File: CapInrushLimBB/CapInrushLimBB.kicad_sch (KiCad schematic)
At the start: 35 parts, among them J1 Screw_Terminal_01x02, J2 Screw_Terminal_01x02, J3 Screw_Terminal_01x02, K1 G5LE-1, Q1 IRF9540N, Q2 Q_PMOS_GDSD, Q3 MPSA42, Q4 MPSA42

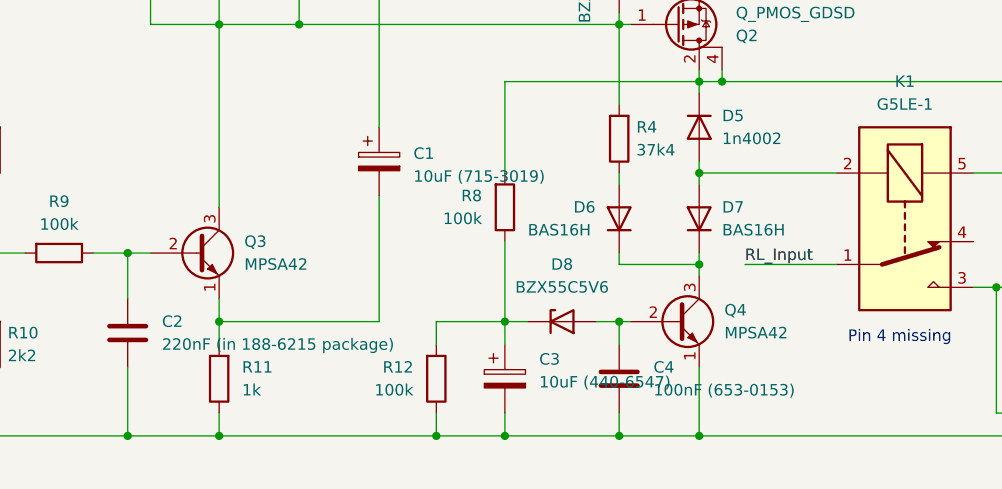
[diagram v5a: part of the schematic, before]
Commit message: Tweaked component values (names) and checked footprints.
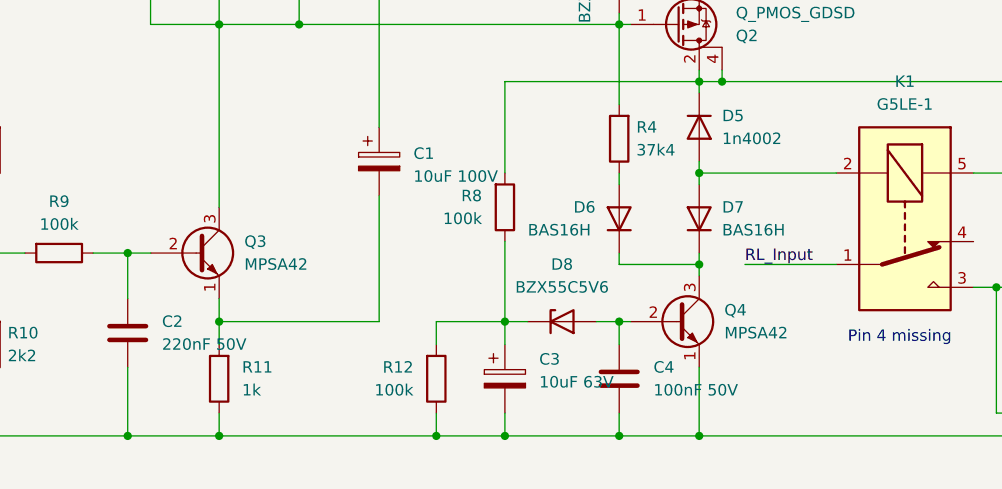
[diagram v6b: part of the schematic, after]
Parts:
- C1: value 10uF (715-3019) -> 10uF 100V
- C2: value 220nF (in 188-6215 package) -> 220nF 50V
- C3: value 10uF (440-6547) -> 10uF 63V
- C4: value 100nF (653-0153) -> 100nF 50V
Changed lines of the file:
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@@
       (effects (font (size 1.27 1.27)) (justify left))
     )
-    (property "Value" "10uF (715-3019)" (id 1) (at 115.57 110.8709 0)
+    (property "Value" "10uF 100V" (id 1) (at 115.57 110.8709 0)
       (effects (font (size 1.27 1.27)) (justify left))
     )
@@
       (effects (font (size 1.27 1.27)) (justify left))
     )
-    (property "Value" "220nF (in 188-6215 package)" (id 1) (at 87.63 129.5399 0)
+    (property "Value" "220nF 50V" (id 1) (at 87.63 129.5399 0)
       (effects (font (size 1.27 1.27)) (justify left))
     )
@@
       (effects (font (size 1.27 1.27)) (justify left))
     )
-    (property "Value" "100nF (653-0153)" (id 1) (at 142.24 134.6199 0)
+    (property "Value" "100nF 50V" (id 1) (at 142.24 134.6199 0)
       (effects (font (size 1.27 1.27)) (justify left))
     )
@@
       (effects (font (size 1.27 1.27)) (justify left))
     )
-    (property "Value" "10uF (440-6547)" (id 1) (at 129.54 133.7309 0)
+    (property "Value" "10uF 63V" (id 1) (at 129.54 133.7309 0)
       (effects (font (size 1.27 1.27)) (justify left))
     )
@@
   (symbol_instances
     (path "/4700c50c-9860-4532-a2c7-53fd9c745d97"
-      (reference "C1") (unit 1) (value "10uF (715-3019)") (footprint "Capacitor_THT:CP_Radial_D6.3mm_P2.50mm")
+      (reference "C1") (unit 1) (value "10uF 100V") (footprint "Capacitor_THT:CP_Radial_D6.3mm_P2.50mm")
     )
     (path "/aa3000e9-ae89-4921-813a-5088ef73c282"
-      (reference "C2") (unit 1) (value "220nF (in 188-6215 package)") (footprint "Capacitor_THT:C_Disc_D5.1mm_W3.2mm_P5.00mm")
+      (reference "C2") (unit 1) (value "220nF 50V") (footprint "Capacitor_THT:C_Disc_D5.1mm_W3.2mm_P5.00mm")
     )
     (path "/d60a5db2-8cd8-4af1-8cbf-01714930ea15"
-      (reference "C3") (unit 1) (value "10uF (440-6547)") (footprint "Capacitor_THT:CP_Radial_D5.0mm_P2.00mm")
+      (reference "C3") (unit 1) (value "10uF 63V") (footprint "Capacitor_THT:CP_Radial_D5.0mm_P2.00mm")
     )
     (path "/c42c87d9-6630-4bdd-b504-0fc4fcaddf1b"
-      (reference "C4") (unit 1) (value "100nF (653-0153)") (footprint "Capacitor_THT:C_Disc_D5.1mm_W3.2mm_P5.00mm")
+      (reference "C4") (unit 1) (value "100nF 50V") (footprint "Capacitor_THT:C_Disc_D5.1mm_W3.2mm_P5.00mm")
     )
     (path "/3d73d65c-87b2-4d45-a3f8-7608125062bc"

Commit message: Started layout.
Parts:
- D5: footprint Diode_THT:D_DO-41_SOD81_P7.62mm_Horizontal -> Diode_THT:D_DO-41_SOD81_P10.16mm_Horizontal
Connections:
- net RL_Input: now also J2.1 (Pin_1); no longer J2.2 (Pin_2)
- net at R5.2: now also J1.2 (Pin_2); no longer J1.1 (Pin_1)
- net at D3.2 (A), Q1.1 (G), Q2.1 (G)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: now also D4.1 (K); no longer D4.2 (A)
- net at D1.2 (A), D3.1 (K), Q1.3 (S)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: now also J1.1 (Pin_1); no longer J1.2 (Pin_2)
- net at C2.2, C3.2, C4.2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: now also J2.2 (Pin_2); no longer J2.1 (Pin_1)
- net at D2.1 (K), Q2.3 (S): now also D4.2 (A); no longer D4.1 (K)
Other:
- moved on the sheet: J1, J2
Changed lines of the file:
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@@
     (pin "2")
   )
-  (symbol (lib_id "Connector:Screw_Terminal_01x02") (at 63.5 91.44 180) (unit 1)
-    (in_bom yes) (on_board yes)
-    (property "Reference" "J1" (id 0) (at 63.5 86.36 0))
-    (property "Value" "Screw_Terminal_01x02" (id 1) (at 55.88 93.98 0))
-    (property "Footprint" "TerminalBlock:TerminalBlock_Altech_AK300-2_P5.00mm" (id 2) (at 63.5 91.44 0)
-      (effects (font (size 1.27 1.27)) hide)
-    )
-    (property "Datasheet" "~" (id 3) (at 63.5 91.44 0)
+  (symbol (lib_id "Connector:Screw_Terminal_01x02") (at 63.5 88.9 0) (mirror y) (unit 1)
+    (in_bom yes) (on_board yes)
+    (property "Reference" "J1" (id 0) (at 63.5 93.98 0))
+    (property "Value" "Screw_Terminal_01x02" (id 1) (at 55.88 86.36 0))
+    (property "Footprint" "TerminalBlock:TerminalBlock_Altech_AK300-2_P5.00mm" (id 2) (at 63.5 88.9 0)
+      (effects (font (size 1.27 1.27)) hide)
+    )
+    (property "Datasheet" "~" (id 3) (at 63.5 88.9 0)
       (effects (font (size 1.27 1.27)) hide)
     )
@@
     (pin "2")
   )
-  (symbol (lib_id "Connector:Screw_Terminal_01x02") (at 38.1 106.68 180) (unit 1)
-    (in_bom yes) (on_board yes)
-    (property "Reference" "J2" (id 0) (at 38.1 101.6 0))
-    (property "Value" "Screw_Terminal_01x02" (id 1) (at 30.48 109.22 0))
-    (property "Footprint" "TerminalBlock:TerminalBlock_Altech_AK300-2_P5.00mm" (id 2) (at 38.1 106.68 0)
-      (effects (font (size 1.27 1.27)) hide)
-    )
-    (property "Datasheet" "~" (id 3) (at 38.1 106.68 0)
+  (symbol (lib_id "Connector:Screw_Terminal_01x02") (at 38.1 104.14 0) (mirror y) (unit 1)
+    (in_bom yes) (on_board yes)
+    (property "Reference" "J2" (id 0) (at 38.1 109.22 0))
+    (property "Value" "Screw_Terminal_01x02" (id 1) (at 30.48 101.6 0))
+    (property "Footprint" "TerminalBlock:TerminalBlock_Altech_AK300-2_P5.00mm" (id 2) (at 38.1 104.14 0)
+      (effects (font (size 1.27 1.27)) hide)
+    )
+    (property "Datasheet" "~" (id 3) (at 38.1 104.14 0)
       (effects (font (size 1.27 1.27)) hide)
     )
@@
     (pin "4")
   )
-  (symbol (lib_id "Device:D_Zener") (at 138.43 88.9 90) (mirror x) (unit 1)
+  (symbol (lib_id "Device:D_Zener") (at 138.43 88.9 90) (unit 1)
     (in_bom yes) (on_board yes)
     (property "Reference" "D4" (id 0) (at 132.08 88.9 0))
@@
       (effects (font (size 1.27 1.27)) (justify left))
     )
-    (property "Footprint" "Diode_THT:D_DO-41_SOD81_P7.62mm_Horizontal" (id 2) (at 147.32 105.41 0)
+    (property "Footprint" "Diode_THT:D_DO-41_SOD81_P10.16mm_Horizontal" (id 2) (at 147.32 105.41 0)
       (effects (font (size 1.27 1.27)) hide)
     )
@@
     )
     (path "/b236afa7-5ddc-4fa0-8b38-6e2f2c55b1a6"
-      (reference "D5") (unit 1) (value "1n4002") (footprint "Diode_THT:D_DO-41_SOD81_P7.62mm_Horizontal")
+      (reference "D5") (unit 1) (value "1n4002") (footprint "Diode_THT:D_DO-41_SOD81_P10.16mm_Horizontal")
     )
     (path "/ddb86822-8413-4e67-8d2a-e7e513335cc0"

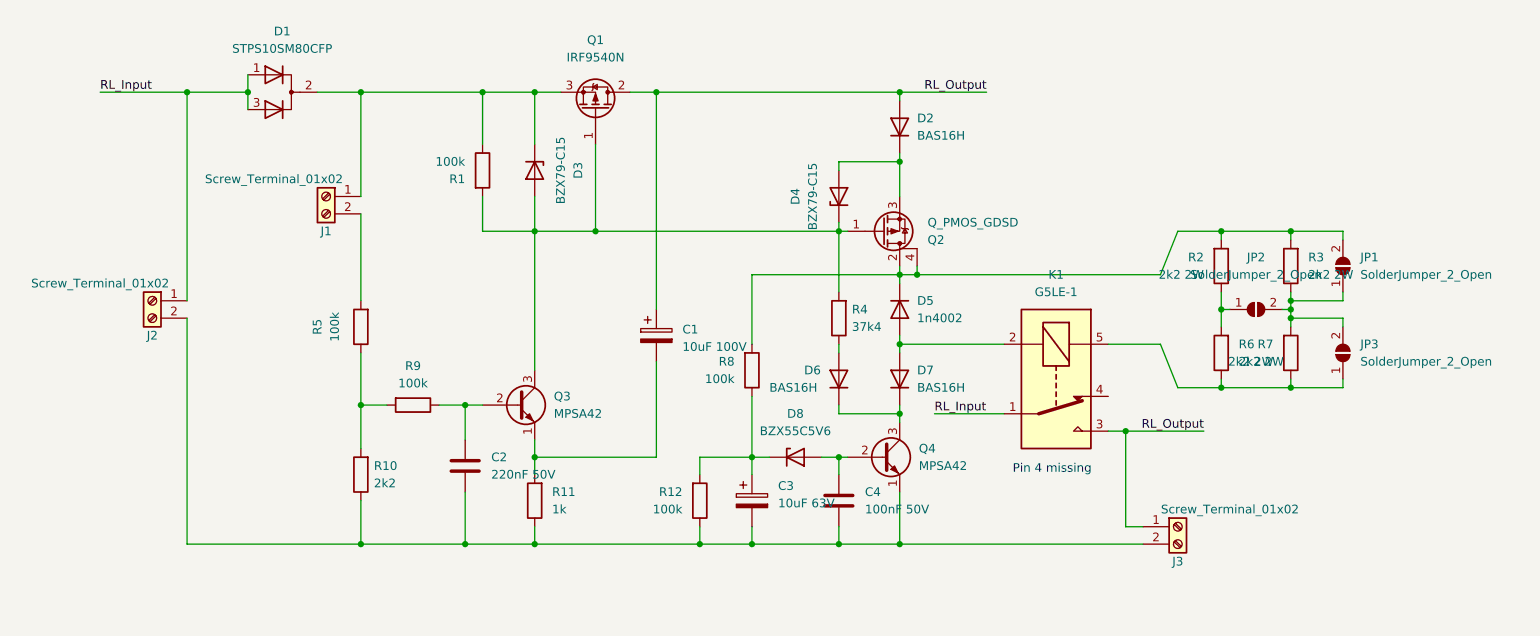
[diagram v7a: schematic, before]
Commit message: Simplified and labelled schematic and performed work on layout.
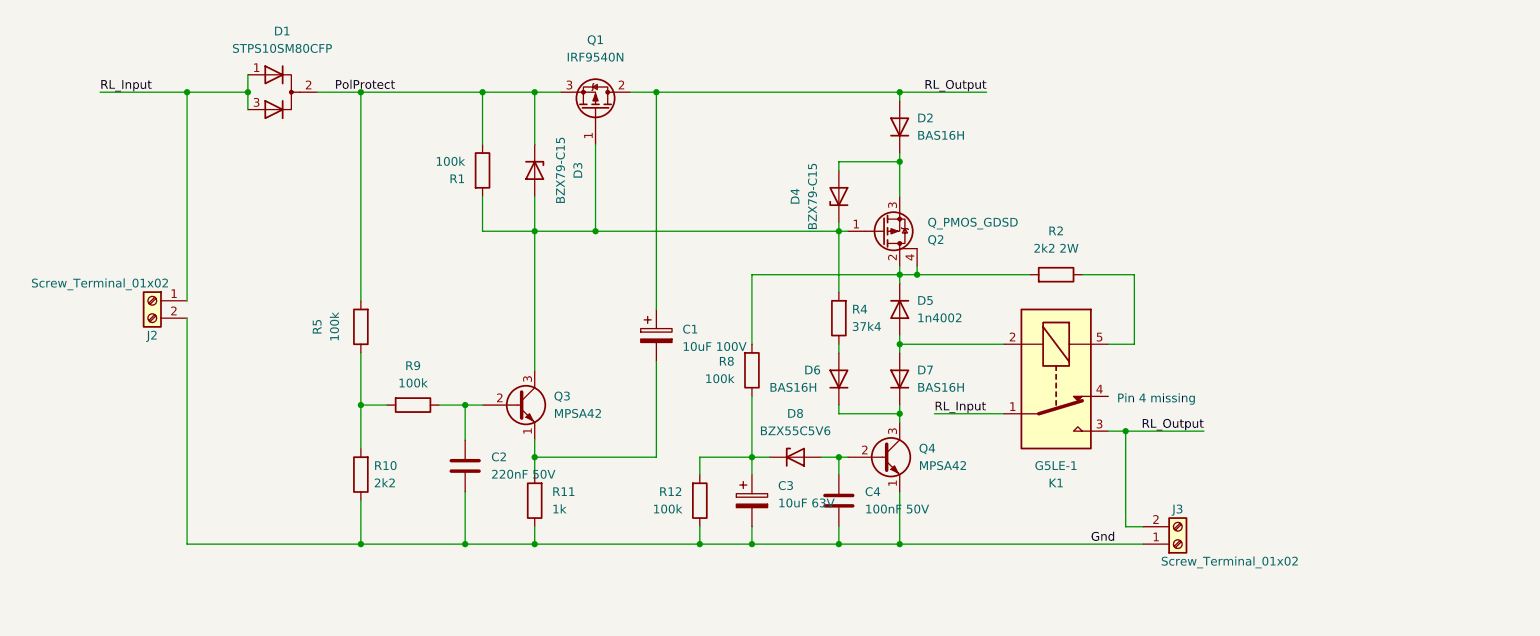
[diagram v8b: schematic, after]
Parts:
- removed J1: Screw_Terminal_01x02, TerminalBlock:TerminalBlock_Altech_AK300-2_P5.00mm, symbol Connector:Screw_Terminal_01x02
- removed JP1, JP2, JP3: SolderJumper_2_Open, Jumper:SolderJumper-2_P1.3mm_Open_Pad1.0x1.5mm, symbol Jumper:SolderJumper_2_Open
- removed R3, R7: 2k2 2W, Resistor_THT:R_Axial_DIN0414_L11.9mm_D4.5mm_P15.24mm_Horizontal, symbol Device:R
- removed R6: 2k2 2W, Resistor_THT:R_Axial_DIN0414_L11.9mm_D4.5mm_P20.32mm_Horizontal, symbol Device:R
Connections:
- net RL_Output: now also J3.2 (Pin_2); no longer J3.1 (Pin_1)
- net PolProtect: now reaches R5.2
- net PolProtect: now also D1.2 (A), D3.1 (K), Q1.3 (S), R1.1
- net Gnd: now reaches C2.2, C3.2, C4.2, J2.2 (Pin_2), Q4.1 (E), R10.1, R11.1, R12.1
- net Gnd: now also J3.1 (Pin_1); no longer J3.2 (Pin_2)
- net at K1.5: now also R2.1
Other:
- moved on the sheet: R2
